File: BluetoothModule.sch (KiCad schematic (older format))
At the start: 10 parts

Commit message: - MAX98089 fertig - Footprints von MAX und Oszilator angepasst - Pullups für I2C hinzugefügt - Bus / Signal Namen Fehlzuweisungen ausgebessert
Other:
- note added: "LED1 und 2 nicht verwenden?\nWarum Temperatur messen?\nUnused Pin Connections nicht beschrieben\nUSB FW Update implementieren?\n\nHat P3_4 internen Pullup? GND -> TEST MODE\nGPIO P3_4 is used to enter Test mode during reset. If the user wants to use this pin to control external\nperipherals, care must be taken to ensure this pin is not pulled LOW and accidentally enters Test mode.\n\nÄnderungen:\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"
- note added: "Wird das Modul als I2S Master betrieben, kann dessen MCLK Ausgang zur Frequenzversorgung des Slaves verwendet werden.\nDies ist hier aber nicht der Fall, daher bleibt MCLK unbeschalten, vgl. DS 6.5\nVermutlich könnte das Modul den MAX98089 mit dem Takt versorgen, so dass der Oszillator für MAX98 entfallen kann\n\nThe BM83 serves as a master to provide clock and frame synchronous signals for the m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"
- note removed: "OUTPUT!!\nvgl. DS 6.5"
- note removed: "The BM83 serves as a master to provide clock and frame synchronous signals for the master/slave data\nsynchronizations, as illustrated in the following figures. The MCLK is optional and is not required if the\nexternal I2S device can drive its system clock on its own.\n\nThe BM83 serves as a slave to receive clock and frame synchronous signals from the external codec or\nDSP devices\n\nMaster CLK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"
- note removed: "Wer ist I2S master??\nLED1 und 2 nicht verwenden?\nWarum Temperatur messen?\nUnused Pin Connections nicht beschrieben\nUSB FW Update implementieren?\n\nHat P3_4 internen Pullup? GND -> TEST MODE\nGPIO P3_4 is used to enter Test mode during reset. If the user wants to use this pin to control external\nperipherals, care must be taken to ensure this pin is not pulled LOW and accidentally enters Test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"
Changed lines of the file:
@@
 Multi-function push button and Power On key
 Text Notes 2200 7400 0    50   ~ 0
-Wer ist I2S master??\nLED1 und 2 nicht verwenden?\nWarum Temperatur messen?\nUnused Pin Connections nicht beschrieben\nUSB FW Update implementieren?\n\nHat P3_4 internen Pullup? GND -> TEST MODE\nGPIO P3_4 is used to enter Test mode during reset. If the user wants to use this pin to control external\nperipherals, care must be taken to ensure this pin is not pulled LOW and accidentally enters Test mode.\n\nÄnderungen:\n- Bypass C an VDD_IO ausgang\n- Bypass C an SYS_PWR\n- Cs für Temperaturmessung hinzugefügt\n- Pullup für active low reset pin
+LED1 und 2 nicht verwenden?\nWarum Temperatur messen?\nUnused Pin Connections nicht beschrieben\nUSB FW Update implementieren?\n\nHat P3_4 internen Pullup? GND -> TEST MODE\nGPIO P3_4 is used to enter Test mode during reset. If the user wants to use this pin to control external\nperipherals, care must be taken to ensure this pin is not pulled LOW and accidentally enters Test mode.\n\nÄnderungen:\n- Bypass C an VDD_IO ausgang\n- Bypass C an SYS_PWR\n- Cs für Temperaturmessung hinzugefügt\n- Pullup für active low reset pin
 $Bitmap
 Pos 9750 5450
@@
 For the I2C, I2S, and UART groups, each respective group's traces should run parallel\nwith as wide spacing as possible and be isolated from other groups with GND copper\nfoil. If isolation is not possible due to limited space, please at least increase the interval\nbetween traces belonging to different groups.
 NoConn ~ 4050 2100
-Text Notes 4550 2200 0    50   ~ 0
-OUTPUT!!\nvgl. DS 6.5
 Text Notes 1550 -150 0    50   ~ 0
-The BM83 serves as a master to provide clock and frame synchronous signals for the master/slave data\nsynchronizations, as illustrated in the following figures. The MCLK is optional and is not required if the\nexternal I2S device can drive its system clock on its own.\n\nThe BM83 serves as a slave to receive clock and frame synchronous signals from the external codec or\nDSP devices\n\nMaster CLK nicht notwendig?\nThis is not part of the I2S standard,[4] \nbut is commonly included for synchronizing \nthe internal operation of the analog/digital converters.\nQuelle: https://en.wikipedia.org/wiki/I%C2%B2S
+Wird das Modul als I2S Master betrieben, kann dessen MCLK Ausgang zur Frequenzversorgung des Slaves verwendet werden.\nDies ist hier aber nicht der Fall, daher bleibt MCLK unbeschalten, vgl. DS 6.5\nVermutlich könnte das Modul den MAX98089 mit dem Takt versorgen, so dass der Oszillator für MAX98 entfallen kann\n\nThe BM83 serves as a master to provide clock and frame synchronous signals for the master/slave data\nsynchronizations, as illustrated in the following figures. The MCLK is optional and is not required if the\nexternal I2S device can drive its system clock on its own.\n\nMaster CLK nicht notwendig?\nThis is not part of the I2S standard,[4] \nbut is commonly included for synchronizing \nthe internal operation of the analog/digital converters.\nQuelle: https://en.wikipedia.org/wiki/I%C2%B2S
 $Comp
 L Device:R R?

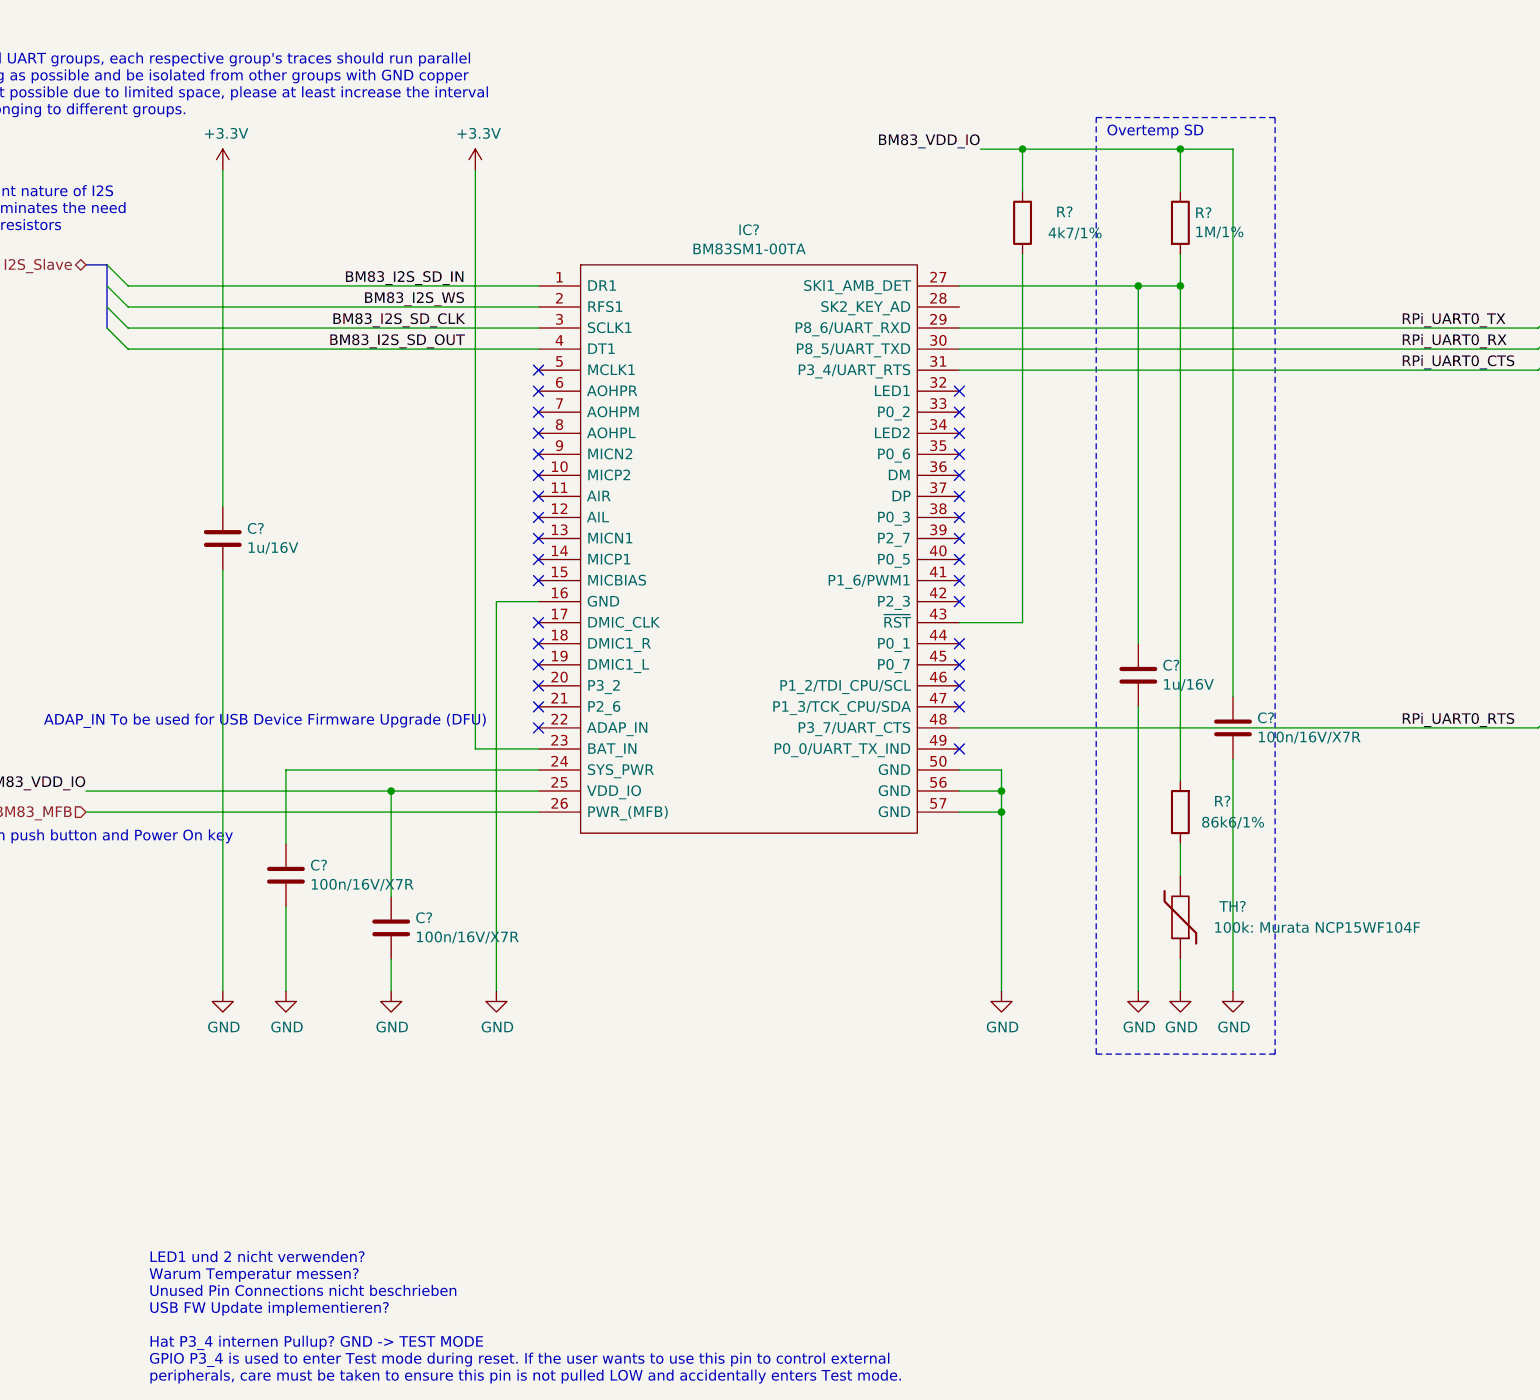
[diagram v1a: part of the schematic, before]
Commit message: - Earth durch GND an den letzten Stellen ersetzt
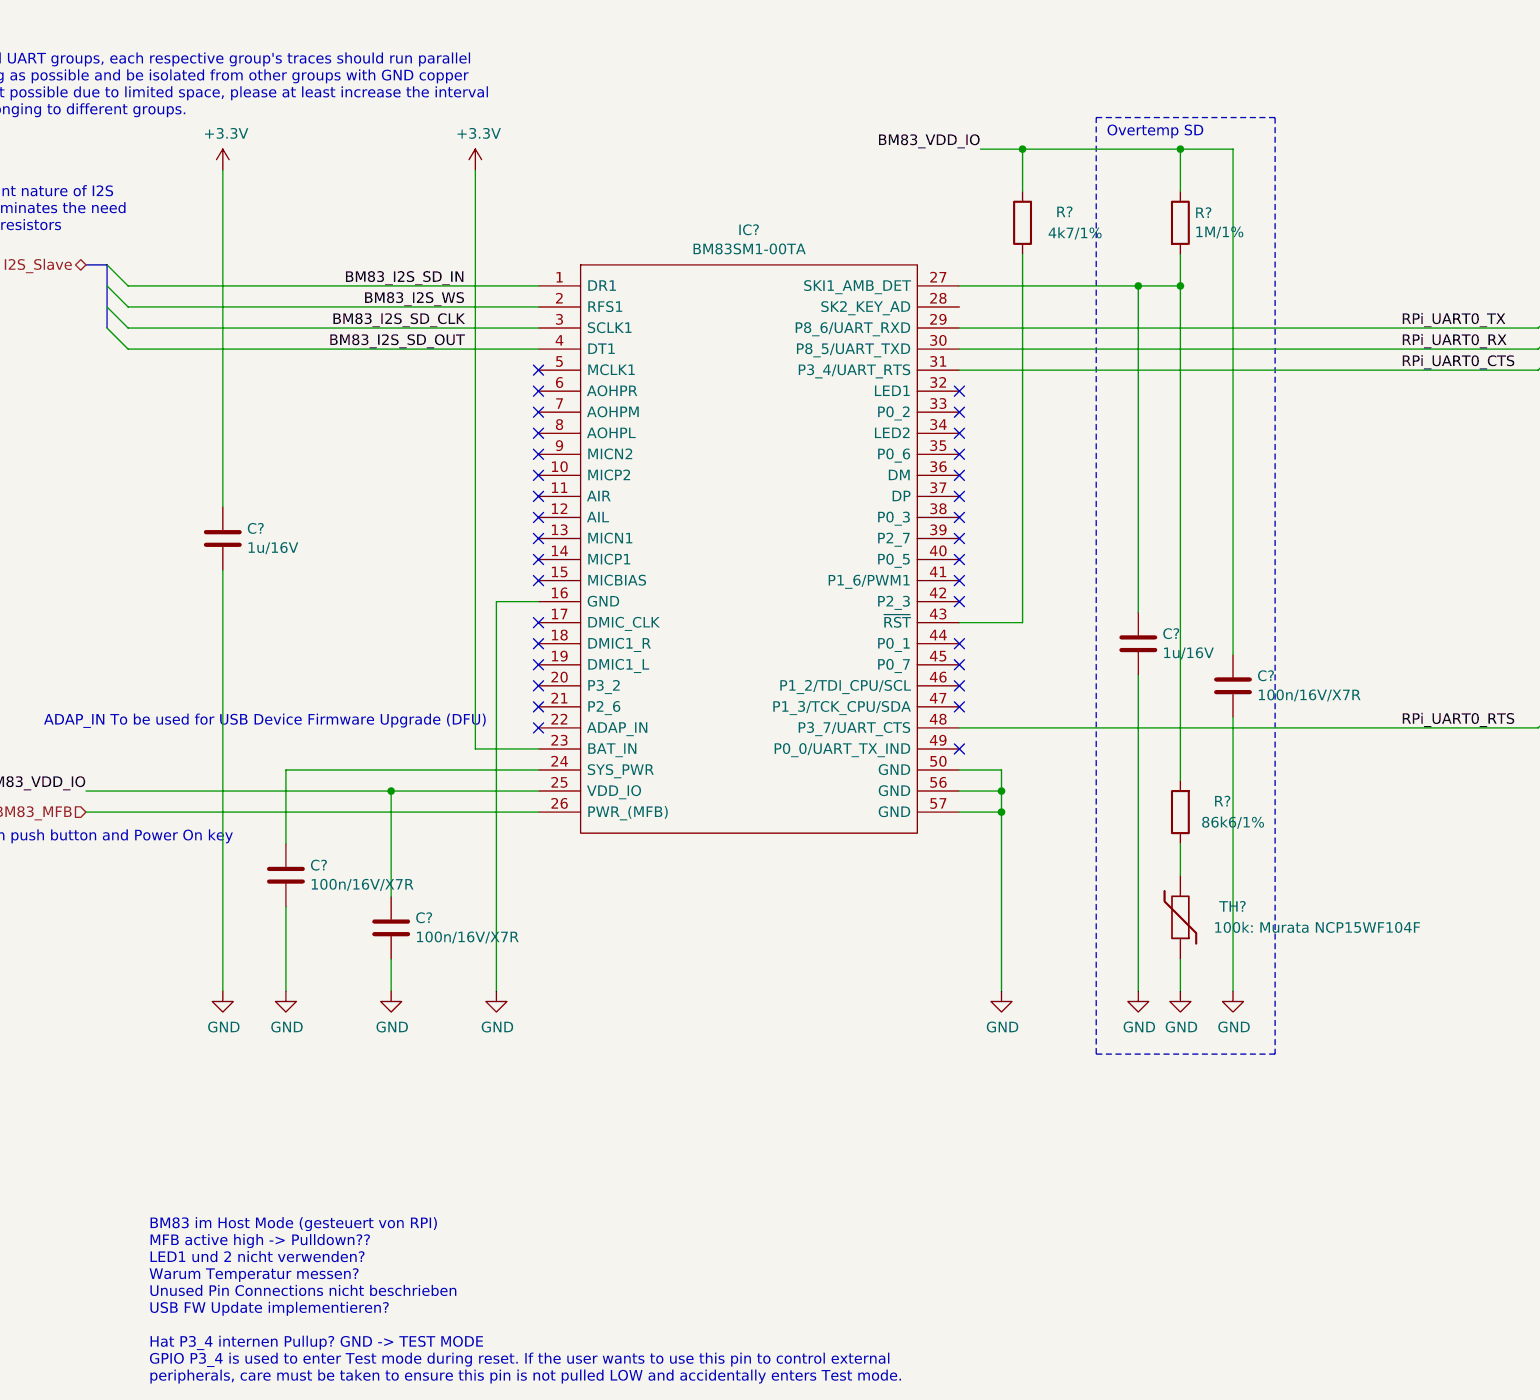
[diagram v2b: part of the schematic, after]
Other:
- note added: "BM83 im Host Mode (gesteuert von RPI)\nMFB active high -> Pulldown??\nLED1 und 2 nicht verwenden?\nWarum Temperatur messen?\nUnused Pin Connections nicht beschrieben\nUSB FW Update implementieren?\n\nHat P3_4 internen Pullup? GND -> TEST MODE\nGPIO P3_4 is used to enter Test mode during reset. If the user wants to use this pin to control external\nperipherals, care must be taken to ensure this pi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"
- note removed: "LED1 und 2 nicht verwenden?\nWarum Temperatur messen?\nUnused Pin Connections nicht beschrieben\nUSB FW Update implementieren?\n\nHat P3_4 internen Pullup? GND -> TEST MODE\nGPIO P3_4 is used to enter Test mode during reset. If the user wants to use this pin to control external\nperipherals, care must be taken to ensure this pin is not pulled LOW and accidentally enters Test mode.\n\nÄnderungen:\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"
- moved on the sheet: C?
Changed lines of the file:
@@
 Multi-function push button and Power On key
 Text Notes 2200 7400 0    50   ~ 0
-LED1 und 2 nicht verwenden?\nWarum Temperatur messen?\nUnused Pin Connections nicht beschrieben\nUSB FW Update implementieren?\n\nHat P3_4 internen Pullup? GND -> TEST MODE\nGPIO P3_4 is used to enter Test mode during reset. If the user wants to use this pin to control external\nperipherals, care must be taken to ensure this pin is not pulled LOW and accidentally enters Test mode.\n\nÄnderungen:\n- Bypass C an VDD_IO ausgang\n- Bypass C an SYS_PWR\n- Cs für Temperaturmessung hinzugefügt\n- Pullup für active low reset pin
+BM83 im Host Mode (gesteuert von RPI)\nMFB active high -> Pulldown??\nLED1 und 2 nicht verwenden?\nWarum Temperatur messen?\nUnused Pin Connections nicht beschrieben\nUSB FW Update implementieren?\n\nHat P3_4 internen Pullup? GND -> TEST MODE\nGPIO P3_4 is used to enter Test mode during reset. If the user wants to use this pin to control external\nperipherals, care must be taken to ensure this pin is not pulled LOW and accidentally enters Test mode.\n\nÄnderungen:\n- Bypass C an VDD_IO ausgang\n- Bypass C an SYS_PWR\n- Cs für Temperaturmessung hinzugefügt\n- Pullup für active low reset pin
 $Bitmap
 Pos 9750 5450
@@
 $EndComp
 Wire Wire Line
-	7350 3650 7350 1050
-Wire Wire Line
-	7350 5050 7350 3950
-Wire Wire Line
 	6900 1700 7100 1700
 Connection ~ 6900 1700
@@
 $Comp
 L Device:C C?
-U 1 1 60DADF73
-P 7350 3800
-F 0 "C?" H 7465 3846 50  0000 L CNN
-F 1 "100n/16V/X7R" H 7465 3755 50  0000 L CNN
-F 2 "Capacitor_SMD:C_0603_1608Metric" H 7388 3650 50  0001 C CNN
-F 3 "~" H 7350 3800 50  0001 C CNN
-	1    7350 3800
-	1    0    0    -1
-$EndComp
-$Comp
-L Device:C C?
 U 1 1 60DAD2BA
-P 6900 3550
-F 0 "C?" H 7015 3596 50  0000 L CNN
-F 1 "1u/16V" H 7015 3505 50  0000 L CNN
-F 2 "Capacitor_SMD:C_0603_1608Metric" H 6938 3400 50  0001 C CNN
-F 3 "~" H 6900 3550 50  0001 C CNN
-	1    6900 3550
+P 6900 3400
+F 0 "C?" H 7015 3446 50  0000 L CNN
+F 1 "1u/16V" H 7015 3355 50  0000 L CNN
+F 2 "Capacitor_SMD:C_0603_1608Metric" H 6938 3250 50  0001 C CNN
+F 3 "~" H 6900 3400 50  0001 C CNN
+	1    6900 3400
 	1    0    0    -1
 $EndComp
@@
 	4050 1700 2100 1700
 Wire Wire Line
-	6900 1700 6900 3400
-Wire Wire Line
-	6900 3700 6900 5050
-Wire Wire Line
-	6050 3800 8800 3800
+	6900 1700 6900 3250
+Wire Wire Line
+	6900 3550 6900 5050
 Wire Wire Line
 	7100 1250 7100 1050
@@
 Wire Wire Line
 	6050 2100 8800 2100
+Wire Wire Line
+	6050 3800 8800 3800
+Wire Wire Line
+	7350 5050 7350 3750
+Wire Wire Line
+	7350 3450 7350 1050
+$Comp
+L Device:C C?
+U 1 1 60DADF73
+P 7350 3600
+F 0 "C?" H 7465 3646 50  0000 L CNN
+F 1 "100n/16V/X7R" H 7465 3555 50  0000 L CNN
+F 2 "Capacitor_SMD:C_0603_1608Metric" H 7388 3450 50  0001 C CNN
+F 3 "~" H 7350 3600 50  0001 C CNN
+	1    7350 3600
+	1    0    0    -1
+$EndComp
 Wire Bus Line
 	2000 1600 2000 1900

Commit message: - BT fertig, warten auf Rueckmeldung von Microchip - CM3 fast fertig - diverse Kleinigkeiten
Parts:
- added D1: LED_BLUE, LED_SMD:LED_0603_1608Metric, symbol Device:LED
- added D2: LED_RED, LED_SMD:LED_0603_1608Metric, symbol Device:LED
- added R12: 10k/5%, Resistor_SMD:R_0603_1608Metric, symbol Device:R
- R10, R11, R9: renamed from R?; footprint (none) -> Resistor_SMD:R_0603_1608Metric
- TH1: renamed from TH?; value 100k: Murata NCP15WF104F -> NTC/100k/1%/4250–4299K; footprint (none) -> Resistor_SMD:R_0603_1608Metric
- U2: renamed from IC?; footprint BM83SM100TA -> TeKaDe:BM83SM1
- gave numbers to parts that had none: 5
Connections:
- net BM83_MFB: now also R12.2
- net GND: now also R12.1
- net SYS_PWR: now reaches C14.1, U2.24 (SYS_PWR)
- net SYS_PWR: now also D1.2 (A), D2.2 (A)
- net at U2.32 (LED1): now also D1.1 (K)
- net at U2.34 (LED2): now also D2.1 (K)
- net BM83_VDD_IO renamed VDD_IO
- net RPi_UART0_CTS: no longer names the net of U2.31 (P3_4/UART_RTS)
- net RPi_UART0_RTS: no longer names the net of U2.48 (P3_7/UART_CTS)
- no-connect marks 33 -> 34
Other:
- note added: "BM83 im Host Mode (gesteuert von RPI)\nKein USB FW update implementiert\n\nÄnderungen:\n- Bypass C an VDD_IO Ausgang\n- Bypass C an SYS_PWR\n- Cs für Temperaturmessung hinzugefuegt\n- Pullup für active low reset pin\n- Pulldown für active high MBR pin (Power Up)\n- CTS / RTS entfernt\n- NTC Thermistor spezifiziert\n- LED1/2 hinzugefuegt\n- Footprint hinzugefuegt\n- Prefix von IC auf U geaendert\n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"
- note added: "For the I2C, I2S, and UART groups, each respective group's traces should run parallel\nwith as wide spacing as possible and be isolated from other groups with GND copper\nfoil. If isolation is not possible due to limited space, please at least increase the \ninterval between traces belonging to different groups."
- note added: "NOTE: (NCP15WF104F03)\nThermistor must be placed close to the\nbattery in the user application for\naccurate measurements and to enable\nthe thermal shutdown feature."
- note added: "Warum Temperatur messen?\nUnused Pin Connections nicht beschrieben\n\nHat P3_4 internen Pullup? GND -> TEST MODE\nGPIO P3_4 is used to enter Test mode during reset. If the user wants to use this pin to control external\nperipherals, care must be taken to ensure this pin is not pulled LOW and accidentally enters Test mode."
- note added: "Wird das Modul als I2S Master betrieben, kann dessen MCLK Ausgang zur Frequenzversorgung \ndes Slaves verwendet werden. Dies ist hier aber nicht der Fall, daher bleibt MCLK unbeschalten.\nvgl. DS 6.5. Vermutlich könnte das Modul den MAX98089 mit dem Takt versorgen, \nso dass der Oszillator für MAX98 entfallen kann\n\nThe BM83 serves as a master to provide clock and frame synchronous signals for t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"
- note removed: "ADAP_IN To be used for USB Device Firmware Upgrade (DFU)"
- note removed: "BM83 im Host Mode (gesteuert von RPI)\nMFB active high -> Pulldown??\nLED1 und 2 nicht verwenden?\nWarum Temperatur messen?\nUnused Pin Connections nicht beschrieben\nUSB FW Update implementieren?\n\nHat P3_4 internen Pullup? GND -> TEST MODE\nGPIO P3_4 is used to enter Test mode during reset. If the user wants to use this pin to control external\nperipherals, care must be taken to ensure this pi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"
- note removed: "For the I2C, I2S, and UART groups, each respective group's traces should run parallel\nwith as wide spacing as possible and be isolated from other groups with GND copper\nfoil. If isolation is not possible due to limited space, please at least increase the interval\nbetween traces belonging to different groups."
- note removed: "Multi-function push button and Power On key"
- note removed: "Wird das Modul als I2S Master betrieben, kann dessen MCLK Ausgang zur Frequenzversorgung des Slaves verwendet werden.\nDies ist hier aber nicht der Fall, daher bleibt MCLK unbeschalten, vgl. DS 6.5\nVermutlich könnte das Modul den MAX98089 mit dem Takt versorgen, so dass der Oszillator für MAX98 entfallen kann\n\nThe BM83 serves as a master to provide clock and frame synchronous signals for the m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"
- moved on the sheet: C11, C12, C13, C14, C15, R10, R11, R9, TH1, U2
